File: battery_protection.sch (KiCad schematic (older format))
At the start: 5 parts, among them Q2 RU8205G, U7 DW01A

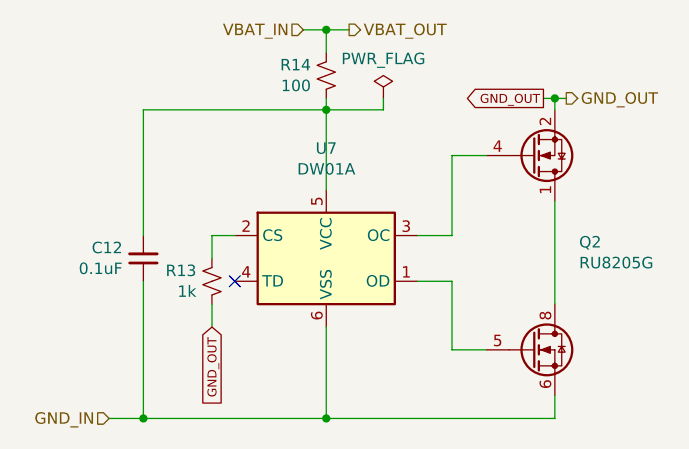
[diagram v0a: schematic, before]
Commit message: clear existing annotations from schematic
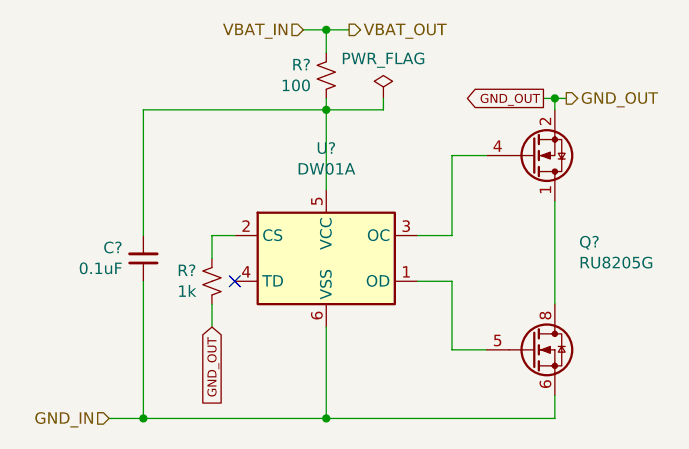
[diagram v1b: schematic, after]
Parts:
- renumbered C12 to C?, Q2 to Q?, R13 to R?, R14 to R?, U7 to U?
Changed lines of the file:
@@
 	2600 2500 2600 2400
 $Comp
-L Device:R_Small_US R13
+L Device:R_Small_US R?
 U 1 1 5C90A25D
 P 2600 2300
-F 0 "R13" H 2532 2254 50  0000 R CNN
+F 0 "R?" H 2532 2254 50  0000 R CNN
 F 1 "1k" H 2532 2345 50  0000 R CNN
 F 2 "Resistor_SMD:R_0603_1608Metric_Pad1.05x0.95mm_HandSolder" H 2600 2300 50  0001 C CNN
@@
 	4100 1500 4150 1500
 $Comp
-L Device:C_Small C12
+L Device:C_Small C?
 U 1 1 5C90E66E
 P 2300 2200
-F 0 "C12" H 2209 2154 50  0000 R CNN
+F 0 "C?" H 2209 2154 50  0000 R CNN
 F 1 "0.1uF" H 2209 2245 50  0000 R CNN
 F 2 "Capacitor_SMD:C_0603_1608Metric_Pad1.05x0.95mm_HandSolder" H 2300 2200 50  0001 C CNN
@@
 $EndComp
 $Comp
-L Device:R_Small_US R14
+L Device:R_Small_US R?
 U 1 1 5C90E934
 P 3100 1400
-F 0 "R14" H 3033 1354 50  0000 R CNN
+F 0 "R?" H 3033 1354 50  0000 R CNN
 F 1 "100" H 3033 1445 50  0000 R CNN
 F 2 "Resistor_SMD:R_0603_1608Metric_Pad1.05x0.95mm_HandSolder" H 3100 1400 50  0001 C CNN
@@
 	2600 2200 2600 2100
 $Comp
-L power:PWR_FLAG #FLG04
+L power:PWR_FLAG #FLG?
 U 1 1 5D69E1EF
 P 3350 1500
-F 0 "#FLG04" H 3350 1575 50  0001 C CNN
+F 0 "#FLG?" H 3350 1575 50  0001 C CNN
 F 1 "PWR_FLAG" H 3350 1673 50  0000 C CNN
 F 2 "" H 3350 1500 50  0001 C CNN
@@
 	3350 1550 3100 1550
 $Comp
-L phone:DW01A U7
+L phone:DW01A U?
 U 1 1 5D6B96F9
 P 3100 2200
-F 0 "U7" H 3100 2681 50  0000 C CNN
+F 0 "U?" H 3100 2681 50  0000 C CNN
 F 1 "DW01A" H 3100 2590 50  0000 C CNN
 F 2 "Package_TO_SOT_SMD:SOT-23-6" H 3100 2200 50  0001 C CNN
@@
 	4100 2400 4100 1950
 $Comp
-L phone:RU8205G Q2
+L phone:RU8205G Q?
 U 1 1 5D6BC1E6
 P 4000 2150
-F 0 "Q2" H 4206 2171 50  0000 L CNN
+F 0 "Q?" H 4206 2171 50  0000 L CNN
 F 1 "RU8205G" H 4206 2080 50  0000 L CNN
 F 2 "Package_SO:TSSOP-8_4.4x3mm_P0.65mm" H 4000 2150 50  0001 C CIN

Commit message: annotate schematic and tweak some footprint associations
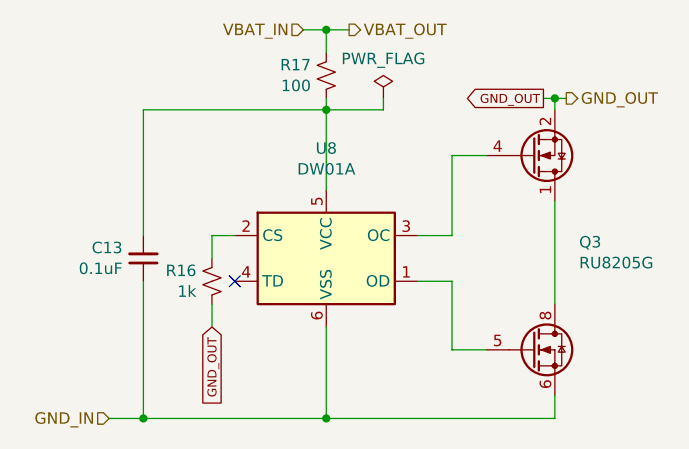
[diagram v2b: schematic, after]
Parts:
- gave numbers to parts that had none: 5
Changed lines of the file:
@@
 	2600 2500 2600 2400
 $Comp
-L Device:R_Small_US R?
+L Device:R_Small_US R16
 U 1 1 5C90A25D
 P 2600 2300
-F 0 "R?" H 2532 2254 50  0000 R CNN
+F 0 "R16" H 2532 2254 50  0000 R CNN
 F 1 "1k" H 2532 2345 50  0000 R CNN
 F 2 "Resistor_SMD:R_0603_1608Metric_Pad1.05x0.95mm_HandSolder" H 2600 2300 50  0001 C CNN
@@
 	4100 1500 4150 1500
 $Comp
-L Device:C_Small C?
+L Device:C_Small C13
 U 1 1 5C90E66E
 P 2300 2200
-F 0 "C?" H 2209 2154 50  0000 R CNN
+F 0 "C13" H 2209 2154 50  0000 R CNN
 F 1 "0.1uF" H 2209 2245 50  0000 R CNN
 F 2 "Capacitor_SMD:C_0603_1608Metric_Pad1.05x0.95mm_HandSolder" H 2300 2200 50  0001 C CNN
@@
 $EndComp
 $Comp
-L Device:R_Small_US R?
+L Device:R_Small_US R17
 U 1 1 5C90E934
 P 3100 1400
-F 0 "R?" H 3033 1354 50  0000 R CNN
+F 0 "R17" H 3033 1354 50  0000 R CNN
 F 1 "100" H 3033 1445 50  0000 R CNN
 F 2 "Resistor_SMD:R_0603_1608Metric_Pad1.05x0.95mm_HandSolder" H 3100 1400 50  0001 C CNN
@@
 	2600 2200 2600 2100
 $Comp
-L power:PWR_FLAG #FLG?
+L power:PWR_FLAG #FLG04
 U 1 1 5D69E1EF
 P 3350 1500
-F 0 "#FLG?" H 3350 1575 50  0001 C CNN
+F 0 "#FLG04" H 3350 1575 50  0001 C CNN
 F 1 "PWR_FLAG" H 3350 1673 50  0000 C CNN
 F 2 "" H 3350 1500 50  0001 C CNN
@@
 	3350 1550 3100 1550
 $Comp
-L phone:DW01A U?
+L phone:DW01A U8
 U 1 1 5D6B96F9
 P 3100 2200
-F 0 "U?" H 3100 2681 50  0000 C CNN
+F 0 "U8" H 3100 2681 50  0000 C CNN
 F 1 "DW01A" H 3100 2590 50  0000 C CNN
 F 2 "Package_TO_SOT_SMD:SOT-23-6" H 3100 2200 50  0001 C CNN
@@
 	4100 2400 4100 1950
 $Comp
-L phone:RU8205G Q?
+L phone:RU8205G Q3
 U 1 1 5D6BC1E6
 P 4000 2150
-F 0 "Q?" H 4206 2171 50  0000 L CNN
+F 0 "Q3" H 4206 2171 50  0000 L CNN
 F 1 "RU8205G" H 4206 2080 50  0000 L CNN
 F 2 "Package_SO:TSSOP-8_4.4x3mm_P0.65mm" H 4000 2150 50  0001 C CIN
